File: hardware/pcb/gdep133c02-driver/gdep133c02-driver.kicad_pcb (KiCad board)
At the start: 4 copper layers, 100 x 80 mm, 133 parts, among them J1 3V3 BENCH ONLY, J2 HOST DIRECT 3V3, Q1 DMN3065LW-7, Q3 MMBT3906-7-F, Q4 DMN3065LW-7, Q6 MMBT3904-7-F, Q7 PJA3433_R1_00001, Q8 DMP3068L-7, U1 0.2 ohm, U2 0.2 ohm, U3 0.2 ohm, U4 TCN75AVOA713, U5 TPS22917DBVR

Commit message: save
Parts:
- added R50: 200k ohm, Driver:R_0805_HandSolder, F.Cu at (136.0, 91.0)
- C26, C27, C33: footprint Driver:Capacitor_SMD__C_0603_1608Metric -> Driver:C_0805_HandSolder
- Q1, Q4: footprint Driver:Package_TO_SOT_SMD__SOT-323_SC-70 -> Driver:SOT323_HandSolder
- R1, R10, R11, R12, R13, R18, R19, R2, R20, R21, R3, R30, R35, R36, R39, R40, R41, R42, R43, R44, R45, R46, R47, R48, R7, R8: footprint Driver:Resistor_SMD__R_0603_1608Metric -> Driver:R_0805_HandSolder
- R17: value 400k ohm -> 200k ohm; footprint Driver:Resistor_SMD__R_0603_1608Metric -> Driver:R_0805_HandSolder
- moved TP26 1.80 mm to (105.0, 97.0)
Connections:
- R17 pad 1: VGL -> VGL_FB_MID
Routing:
- net VBB_3P5V: track 154.4 -> 128.2 mm
- net EPD_3V3: track 680.0 -> 700.4 mm, vias 18 -> 24
- net CS_S_N: track 74.8 -> 93.0 mm, vias 3 -> 4
- net HOST_RES_N: track 18.7 -> 33.3 mm
- net GND: track 420.9 -> 407.7 mm
- net VDDP: track 98.8 -> 111.5 mm, vias 4 -> 6
- net Q7_GATE: track 12.4 -> 18.5 mm, vias 2 -> 3
- net VGH: track 127.8 -> 131.5 mm, vias 4 -> 6
- net VGL: track 72.8 -> 69.4 mm, vias 4 -> 8
- net VGL_FB_MID: track 0.00 -> 3.00 mm
- net HOST_SCLK: track 24.9 -> 26.3 mm, vias 0 -> 2
- net VCC: track 72.0 -> 72.7 mm, vias 3 -> 7

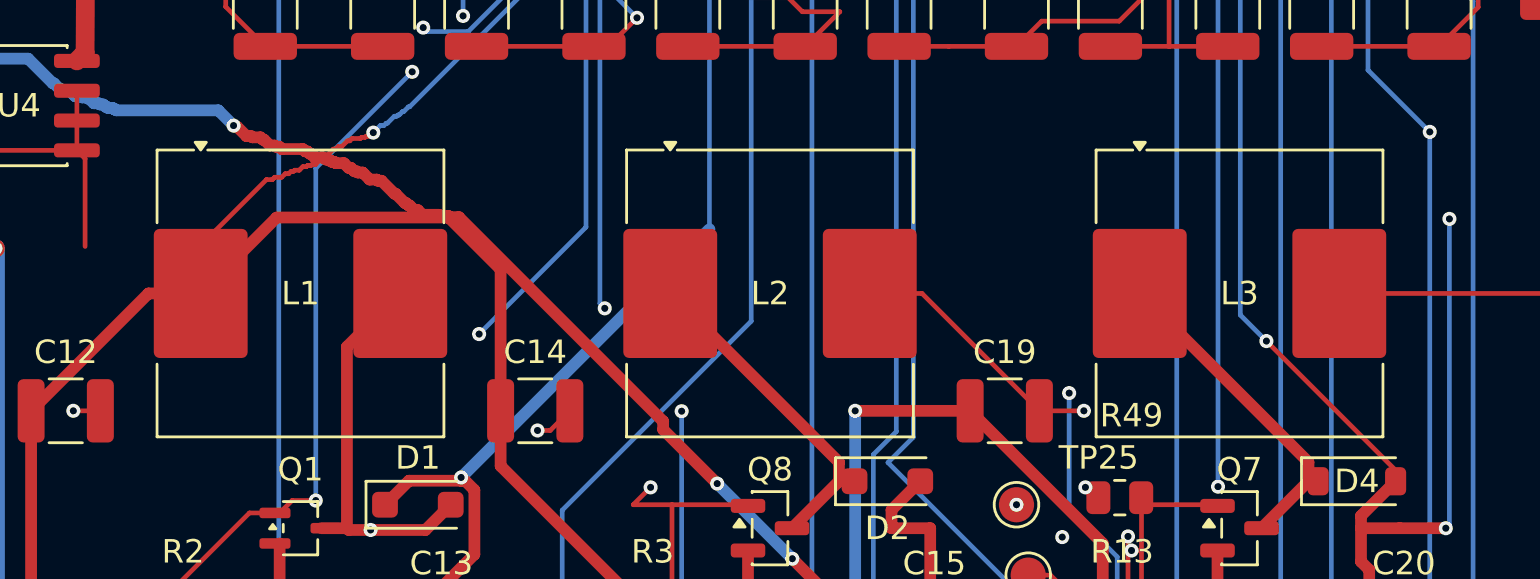
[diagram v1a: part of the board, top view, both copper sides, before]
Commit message: feat(pcb): release v0.9 with fee-waived resistor selections
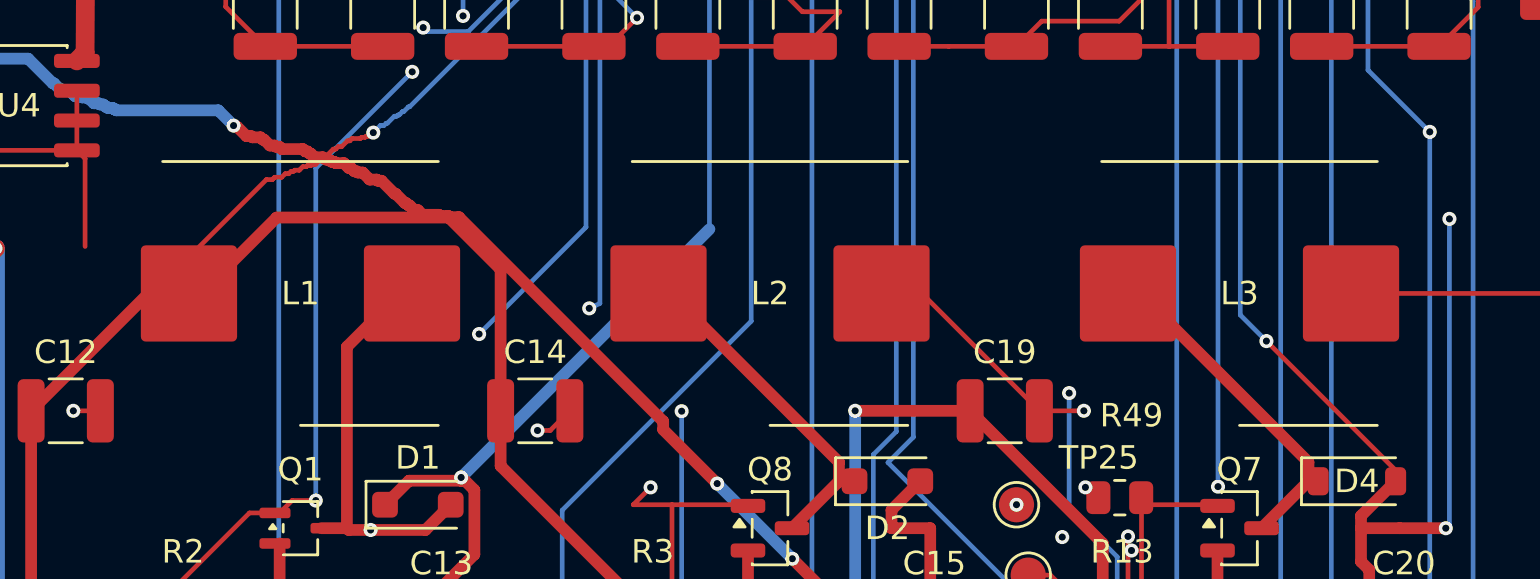
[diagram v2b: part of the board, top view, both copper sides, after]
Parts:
- C28: value 2.2uF/50V -> 4.7uF/50V
- D3, D5, D6: value BAT54S-7-F -> BAT54SLT1G
- L1, L2, L3: footprint Driver:Inductor_SMD__L_Coilcraft_MSS1246T-XXX -> Driver:L_JIERR_PCR1040
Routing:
- net RESEN: track 60.1 -> 60.8 mm

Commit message: hardware: use Murata C440198 0805 capacitors and release v0.10
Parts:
- C1, C103, C104, C106, C107, C109, C110, C112, C113, C115, C116, C118, C119, C13, C15, C2, C20, C3, C4, C5, C6, C7: value 10uF/50V -> 10uF/50V X5R; footprint Driver:Capacitor_SMD__C_1210_3225Metric -> Driver:C_0805_HandSolder
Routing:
- net VSNH: track 47.0 -> 39.8 mm, vias 0 -> 2
- net GND: track 407.7 -> 403.7 mm
- net RESEP: track 54.6 -> 52.5 mm
- net GDRC: track 56.8 -> 54.9 mm, vias 4 -> 7

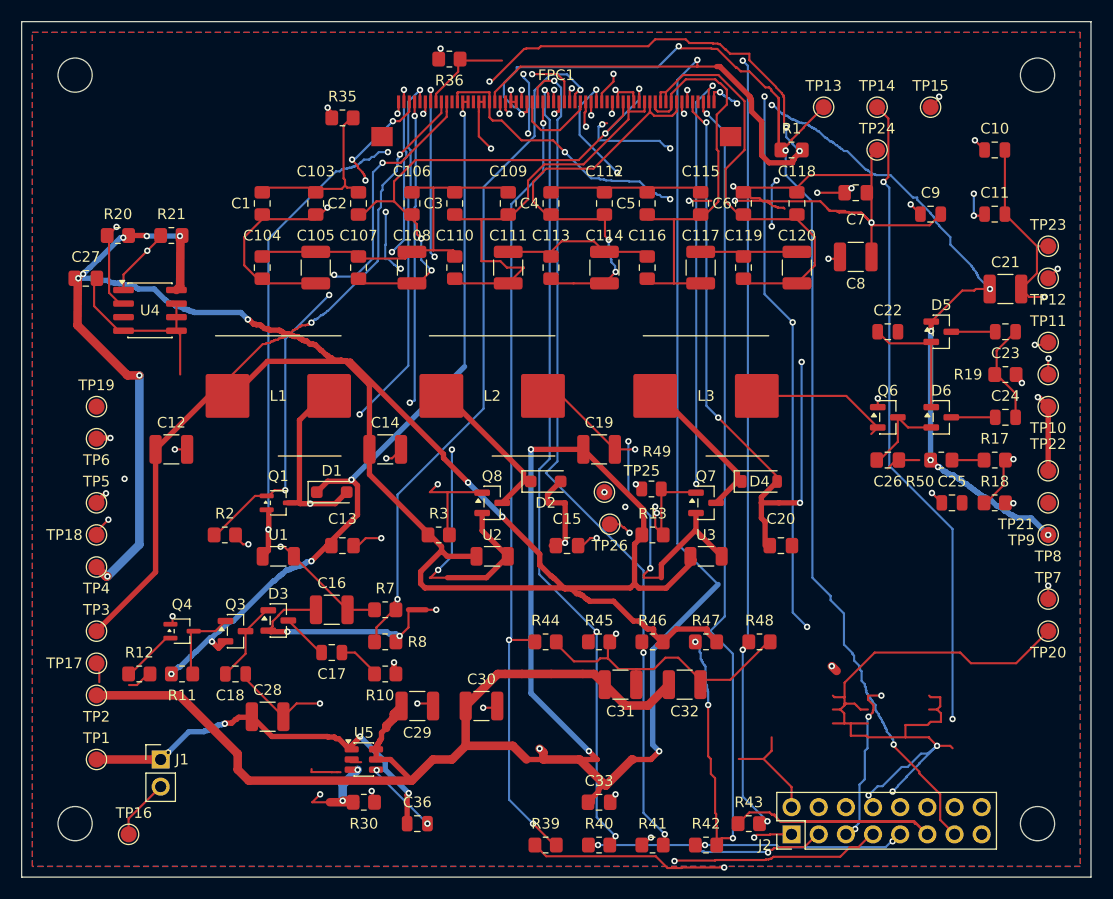
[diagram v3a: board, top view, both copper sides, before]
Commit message: feat(pcb): adopt 17 basic-library groups and release v0.11 prototype
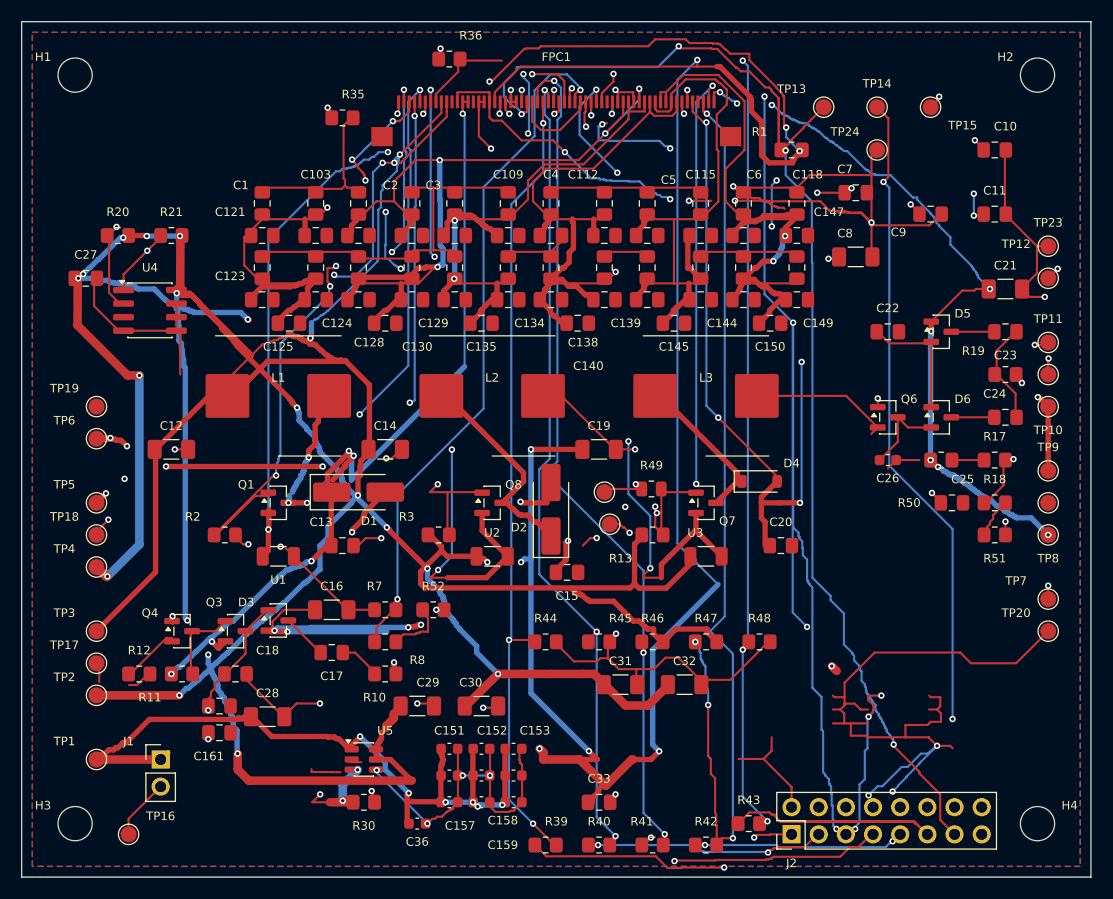
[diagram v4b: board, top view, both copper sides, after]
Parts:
- added C121: 1uF/50V, Driver:C_0805_HandSolder, F.Cu at (72.5, 70.0)
- added C122: 1uF/50V, Driver:C_0805_HandSolder, F.Cu at (77.5, 70.0)
- added C123: 100nF/100V, Driver:C_0805_HandSolder, F.Cu at (72.5, 76.0)
- added C124: 100nF/100V, Driver:C_0805_HandSolder, F.Cu at (77.5, 76.0)
- added C125: 100nF/100V, Driver:C_0805_HandSolder, F.Cu at (75.0, 78.2)
- added C126: 1uF/50V, Driver:C_0805_HandSolder, F.Cu at (81.5, 70.0)
- added C127: 1uF/50V, Driver:C_0805_HandSolder, F.Cu at (86.5, 70.0)
- added C128: 100nF/100V, Driver:C_0805_HandSolder, F.Cu at (81.5, 76.0)
- added C129: 100nF/100V, Driver:C_0805_HandSolder, F.Cu at (86.5, 76.0)
- added C130: 100nF/100V, Driver:C_0805_HandSolder, F.Cu at (84.0, 78.2)
- added C131: 1uF/50V, Driver:C_0805_HandSolder, F.Cu at (90.5, 70.0)
- added C132: 1uF/50V, Driver:C_0805_HandSolder, F.Cu at (95.5, 70.0)
- added C133: 100nF/100V, Driver:C_0805_HandSolder, F.Cu at (90.5, 76.0)
- added C134: 100nF/100V, Driver:C_0805_HandSolder, F.Cu at (95.5, 76.0)
- added C135: 100nF/100V, Driver:C_0805_HandSolder, F.Cu at (93.0, 78.2)
- added C136: 1uF/50V, Driver:C_0805_HandSolder, F.Cu at (99.5, 70.0)
- added C137: 1uF/50V, Driver:C_0805_HandSolder, F.Cu at (104.5, 70.0)
- added C138: 100nF/100V, Driver:C_0805_HandSolder, F.Cu at (99.5, 76.0)
- added C139: 100nF/100V, Driver:C_0805_HandSolder, F.Cu at (104.5, 76.0)
- added C140: 100nF/100V, Driver:C_0805_HandSolder, F.Cu at (102.0, 78.2)
- added C141: 1uF/50V, Driver:C_0805_HandSolder, F.Cu at (108.5, 70.0)
- added C142: 1uF/50V, Driver:C_0805_HandSolder, F.Cu at (113.5, 70.0)
- added C143: 100nF/100V, Driver:C_0805_HandSolder, F.Cu at (108.5, 76.0)
- added C144: 100nF/100V, Driver:C_0805_HandSolder, F.Cu at (113.5, 76.0)
- added C145: 100nF/100V, Driver:C_0805_HandSolder, F.Cu at (111.0, 78.2)
- added C146: 1uF/50V, Driver:C_0805_HandSolder, F.Cu at (117.5, 70.0)
- added C147: 1uF/50V, Driver:C_0805_HandSolder, F.Cu at (122.5, 70.0)
- added C148: 100nF/100V, Driver:C_0805_HandSolder, F.Cu at (117.5, 76.0)
- added C149: 100nF/100V, Driver:C_0805_HandSolder, F.Cu at (122.5, 76.0)
- added C150: 100nF/100V, Driver:C_0805_HandSolder, F.Cu at (120.0, 78.2)
- added C151: 100pF/50V C0G, Driver:Capacitor_SMD__C_0603_1608Metric, F.Cu at (90.0, 118.0)
- added C152: 100pF/50V C0G, Driver:Capacitor_SMD__C_0603_1608Metric, F.Cu at (93.0, 118.0)
- added C153: 100pF/50V C0G, Driver:Capacitor_SMD__C_0603_1608Metric, F.Cu at (96.0, 118.0)
- added C154: 100pF/50V C0G, Driver:Capacitor_SMD__C_0603_1608Metric, F.Cu at (90.0, 120.5)
- added C155: 100pF/50V C0G, Driver:Capacitor_SMD__C_0603_1608Metric, F.Cu at (93.0, 120.5)
- added C156: 100pF/50V C0G, Driver:Capacitor_SMD__C_0603_1608Metric, F.Cu at (96.0, 120.5)
- added C157: 100pF/50V C0G, Driver:Capacitor_SMD__C_0603_1608Metric, F.Cu at (90.0, 123.0)
- added C158: 100pF/50V C0G, Driver:Capacitor_SMD__C_0603_1608Metric, F.Cu at (93.0, 123.0)
- added C159: 100pF/50V C0G, Driver:Capacitor_SMD__C_0603_1608Metric, F.Cu at (96.0, 123.0)
- added C160: 100nF/100V, Driver:C_0805_HandSolder, F.Cu at (68.5, 114.0)
- added C161: 22nF/50V, Driver:C_0805_HandSolder, F.Cu at (68.5, 116.5)
- added R51: 1k ohm, Driver:R_0805_HandSolder, F.Cu at (141.0, 98.0)
- added R52: 10k ohm, Driver:R_0805_HandSolder, F.Cu at (88.5, 105.0)
- C10, C11, C17, C22, C23, C24, C25, C9: footprint Driver:Capacitor_SMD__C_0805_2012Metric -> Driver:C_0805_HandSolder
- C105, C108, C111, C114, C117, C120: value 3.3uF/50V -> 1uF/50V; footprint Driver:Capacitor_SMD__C_1210_3225Metric -> Driver:C_0805_HandSolder
- C12, C14, C16, C19, C21, C28, C29, C30, C31, C32, C8: footprint Driver:Capacitor_SMD__C_1210_3225Metric -> Driver:C_1206_HandSolder
- C18: value 220nF/50V -> 100nF/100V; footprint Driver:Capacitor_SMD__C_0805_2012Metric -> Driver:C_0805_HandSolder
- C26: footprint Driver:C_0805_HandSolder -> Driver:Capacitor_SMD__C_0603_1608Metric
- C27, C33: value 100nF/50V -> 100nF/100V
- C36: value 1nF/50V C0G -> 100pF/50V C0G; footprint Driver:Capacitor_SMD__C_0805_2012Metric -> Driver:Capacitor_SMD__C_0603_1608Metric
- D1, D2: value MBR230S1F-7 -> SS34; footprint Driver:Diode_SMD__D_SOD-123F -> Driver:D_SMA_HandSolder
- D4: value B0530W-7-F -> B5819W SL
- Q1, Q4: value DMN3065LW-7 -> AO3400A; footprint Driver:SOT323_HandSolder -> Driver:Package_TO_SOT_SMD__SOT-23
- Q6: value MMBT3904-7-F -> MMBT3904
- Q7: value PJA3433_R1_00001 -> AO3401A
- Q8: value DMP3068L-7 -> AO3401A
- R18: value 16k ohm -> 15k ohm
- R8: value 110k ohm -> 100k ohm
- moved D2 2.65 mm to (99.5, 95.6), turned to 90 degrees
- moved C15 2.50 mm to (101.0, 101.5)
- moved D1 2.50 mm to (81.5, 94.0)
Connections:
- R18 pad 2: REG_VGN -> R18_FB_MID
- R8 pad 2: VGH -> R8_FB_MID
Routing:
- net EPD_3V3: track 700.4 -> 759.9 mm, vias 24 -> 35
- net SI1: track 99.3 -> 149.5 mm, vias 7 -> 8
- net VDDN: track 98.8 -> 138.0 mm, vias 3 -> 7
- net BENCH_3V3: track 38.4 -> 70.2 mm, vias 4 -> 6
- net SW_CT: track 7.04 -> 33.0 mm, vias 2 -> 4
- net VSPL: track 53.1 -> 77.3 mm
- net VSNL2: track 41.2 -> 59.8 mm, vias 0 -> 2
- net VSNH: track 39.8 -> 54.8 mm, vias 2 -> 1
- net VSPH: track 56.1 -> 70.6 mm
- net VSNL: track 39.2 -> 53.0 mm
- net VSPL2: track 40.4 -> 50.9 mm, vias 0 -> 2
- net VGH: track 131.5 -> 140.4 mm, vias 6 -> 8
- net PUMP_P_LOW: track 7.71 -> 15.0 mm, vias 0 -> 2
- net GDRP: track 57.8 -> 64.7 mm, vias 4 -> 5
- net VDDP: track 111.5 -> 104.8 mm, vias 6 -> 7
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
